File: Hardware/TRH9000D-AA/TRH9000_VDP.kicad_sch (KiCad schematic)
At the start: 15 parts, among them U1 V9990, U2 KM428C256, U3 KM428C256, U9 SST39SF010A-lrj, X1 Crystek_CE3291, Y1 Y_HCM4921477270ABJT

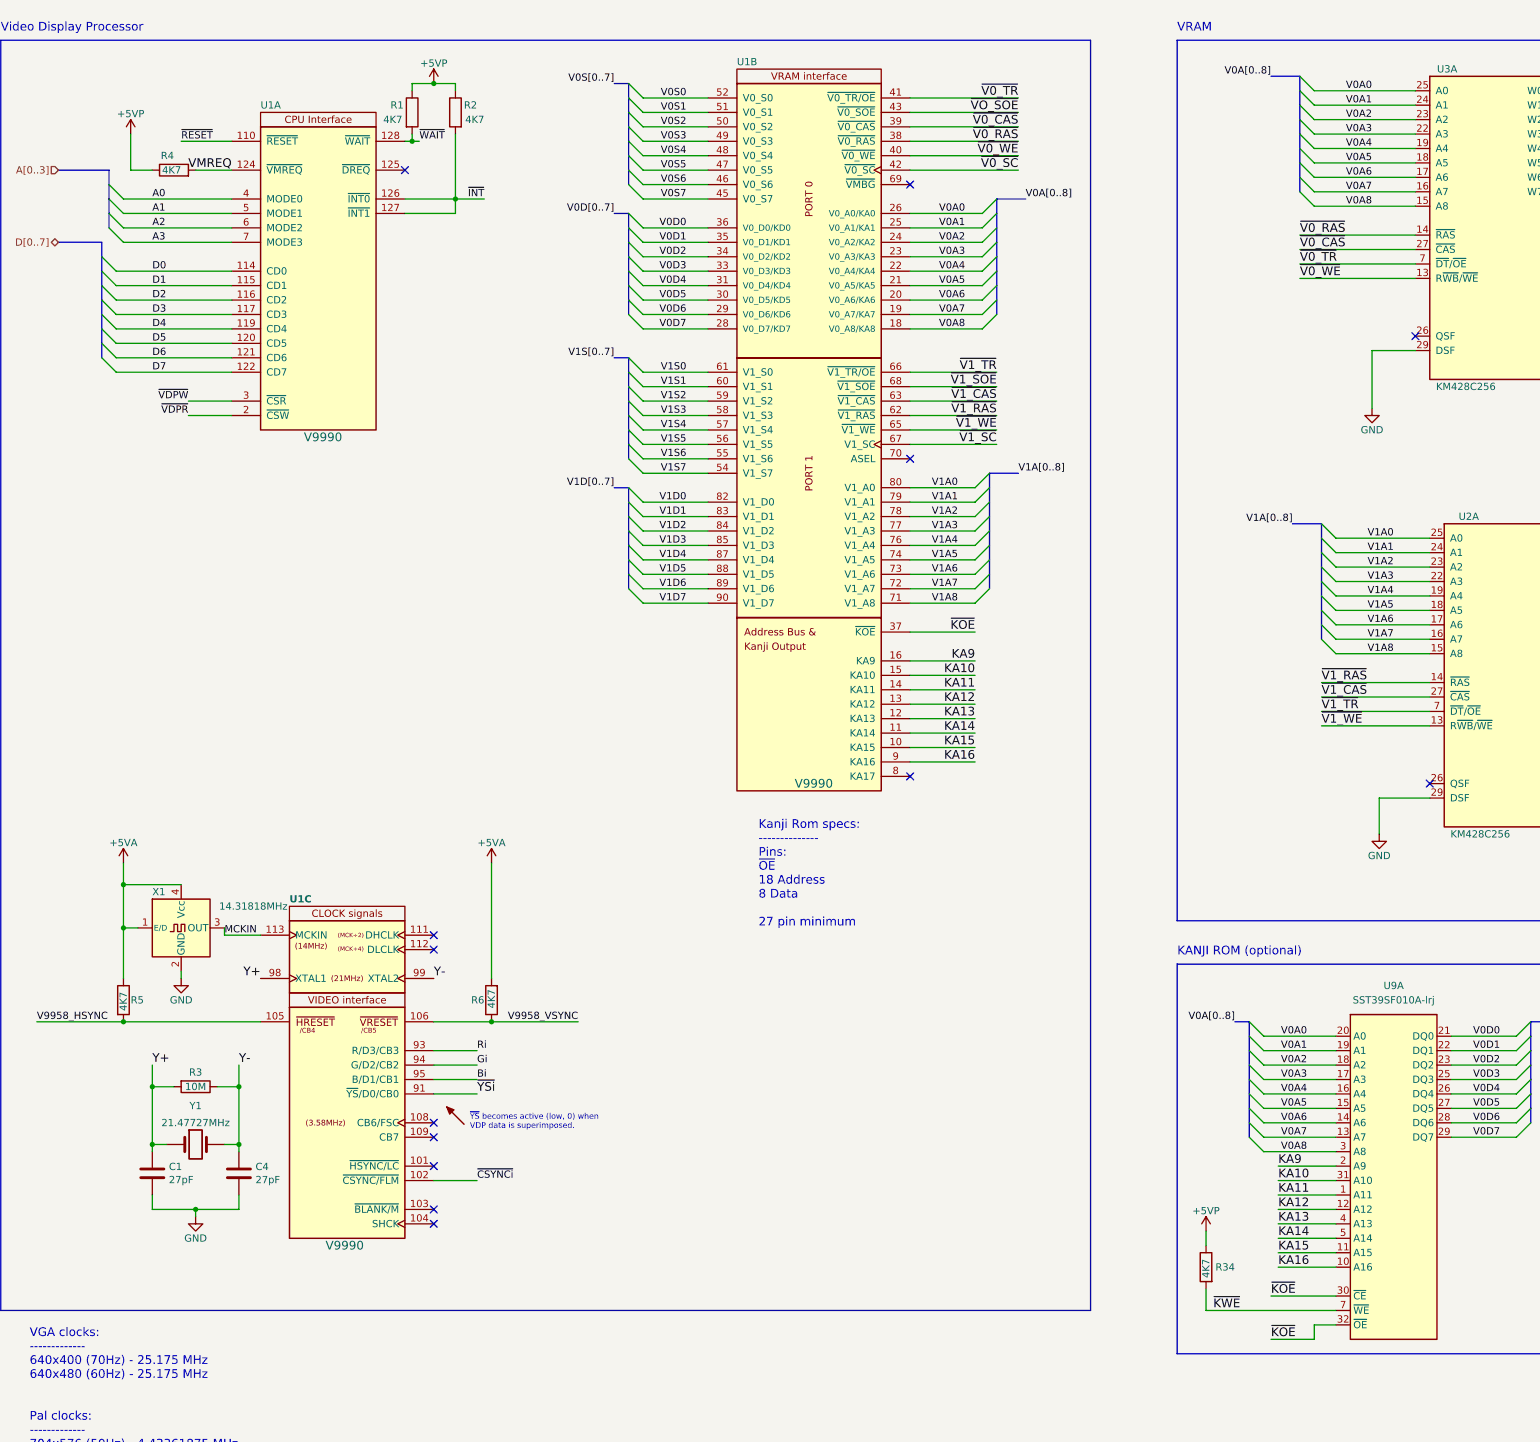
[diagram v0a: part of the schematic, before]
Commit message: Finished rerouting the AA-variant, and replaced the fuses with SMD-ones.
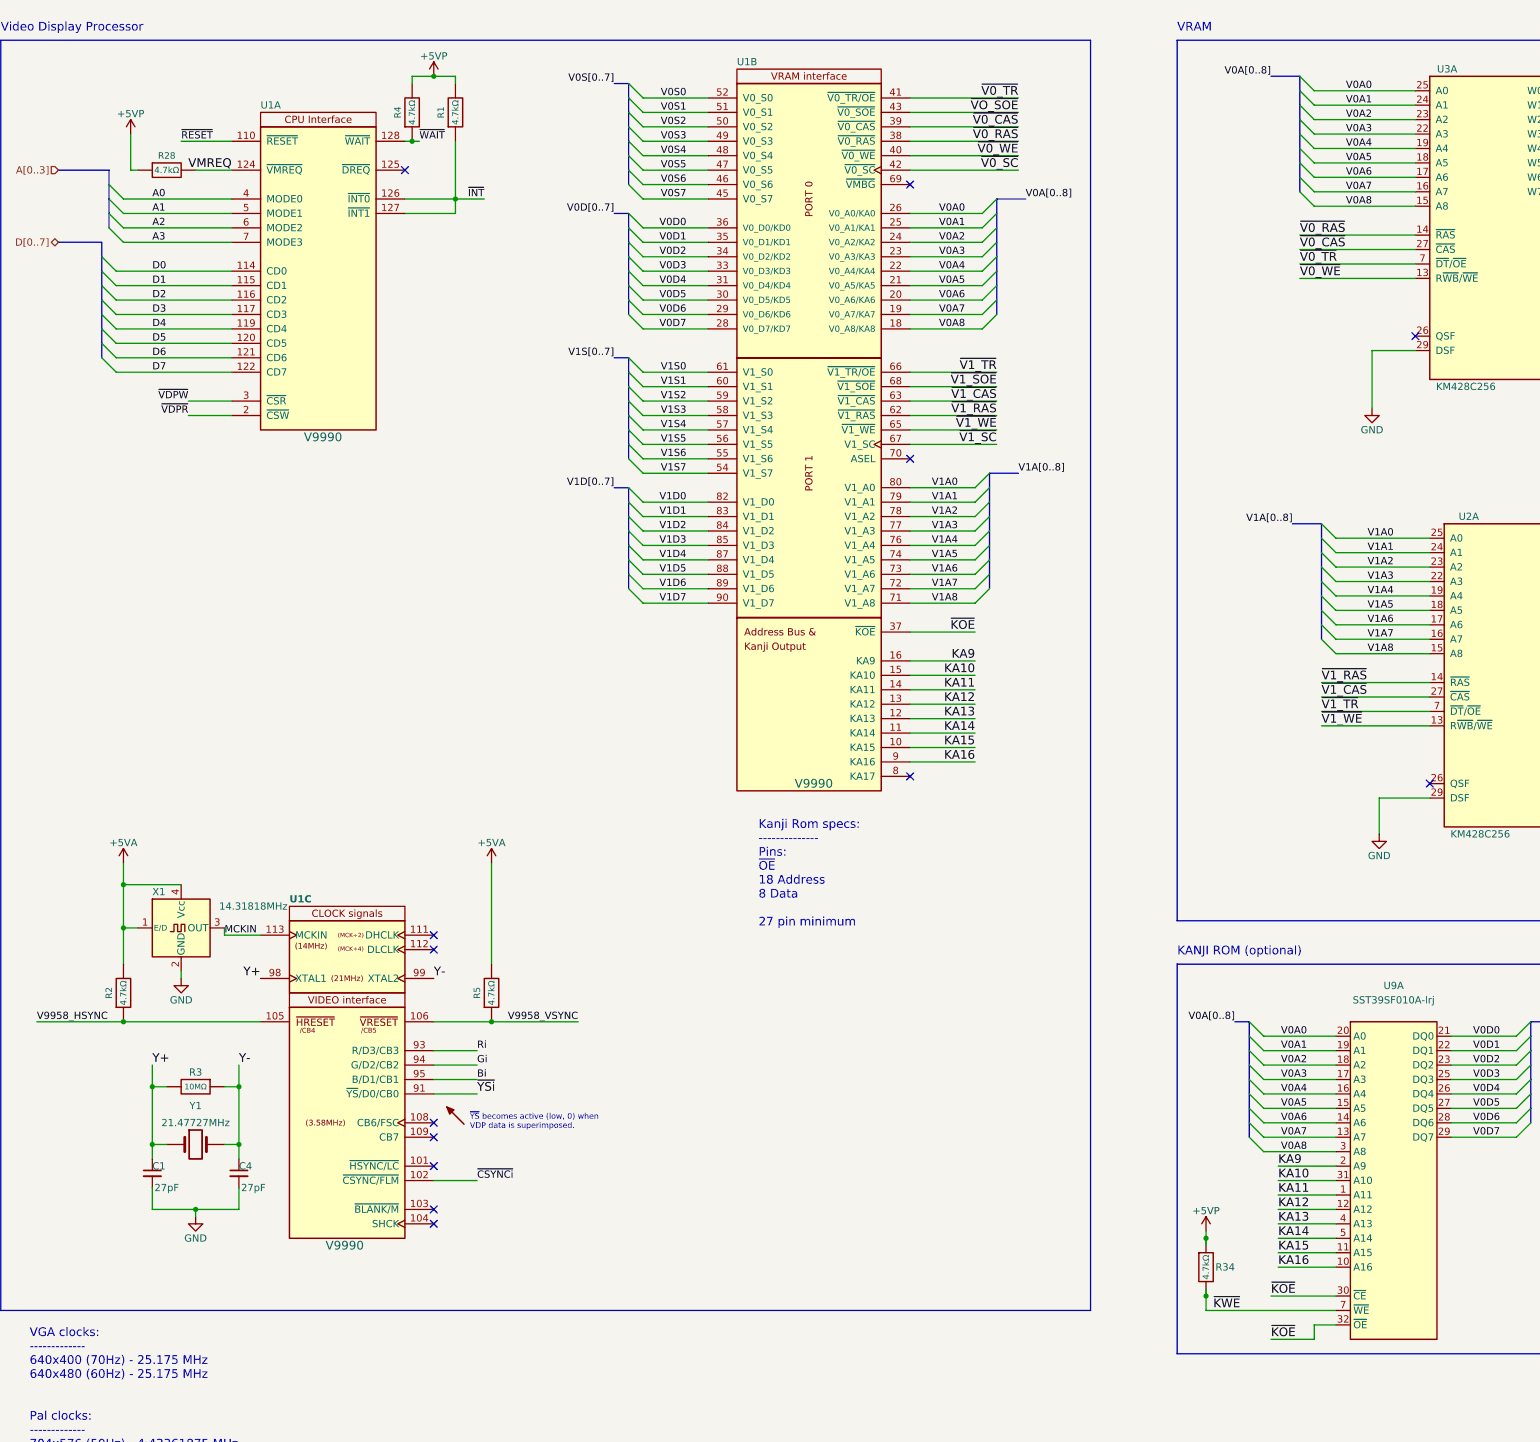
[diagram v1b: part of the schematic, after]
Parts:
- removed R1, R2, R4, R5, R6: 4K7, Resistor_SMD:R_0805_2012Metric, symbol Device:R
- added R1, R2, R28, R4, R5: R_RC0603FR-074K7L, Resistor_SMD:R_0603_1608Metric, symbol LRJ-parts:R_RC0603FR-074K7L
- C1, C4: value 27pF -> C_CL21B474KOFNNNG; footprint Capacitor_SMD:C_0805_2012Metric -> Capacitor_SMD:C_0603_1608Metric_Pad1.08x0.95mm_HandSolder; symbol Device:C -> LRJ-parts:C_CL10C270JB8NNNC; Capacitance (none) -> 27pF; MPN (none) -> CL10C270JB8NNNC; Manufacturer (none) -> Samsung Electro-Mechanics; Tolerance (none) -> ±5%; Voltage rating (none) -> 50V
- R3: value 10M -> R_RC0603FR-0710KL; footprint Resistor_SMD:R_0805_2012Metric -> LRJ:R_0603_1608Metric_roundcourt; symbol Device:R -> LRJ-parts:R_RC0603FR-0710ML; MPN (none) -> RC0603FR-0710ML; Manufacturer (none) -> Yageo; Operating Temperature  (none) -> -55°C to 155°C; Power Rating (none) -> 0.1W; Resistance (none) -> 10MΩ
- R34: value 4K7 -> R_RC0603FR-074K7L; footprint Resistor_SMD:R_0805_2012Metric -> Resistor_SMD:R_0603_1608Metric; symbol Device:R -> LRJ-parts:R_RC0603FR-074K7L; MPN (none) -> RC0603FR-074K7L; Manufacturer (none) -> Yageo; Power Rating (none) -> 0.1W; Resistance (none) -> 4.7kΩ
- Y1: footprint trh9000:Crystal_HC49-US_Vertical_cy_mod -> LRJ:Crystal_HC49-US_Vertical
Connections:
- net +5VA: now also R2.2, R5.2
- net +5VP: now also R1.2, R28.1, R4.2
- net V9958_HSYNC: now also R2.1
- net V9958_VSYNC: now also R5.1
- net VMREQ: now also R28.2
- net Y+: now also R3.1; no longer R3.2
- net Y-: now also R3.2; no longer R3.1
- net ~{INT}: now also R1.1
- net ~{WAIT}: now also R4.1
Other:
- moved on the sheet: R34, U9A
